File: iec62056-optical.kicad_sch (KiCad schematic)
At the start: 5 parts, among them J1 Conn_01x04_Male, Q1 Q_Photo_NPN

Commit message: version 1.0
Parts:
- D1: value LED -> IR42-21C; LCSC (none) -> C131198
- Q1: value Q_Photo_NPN -> PT42-21B; LCSC (none) -> C131199
- R1: value R -> 22R; LCSC (none) -> C23345
- R2: value R -> 1k8; LCSC (none) -> C4177
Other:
- moved on the sheet: D1, Q1, R1, R2

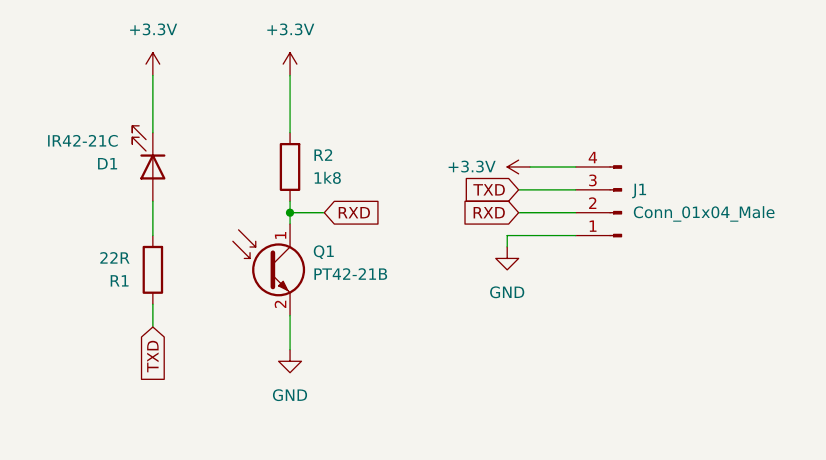
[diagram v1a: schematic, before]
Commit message: oprava orientace diody
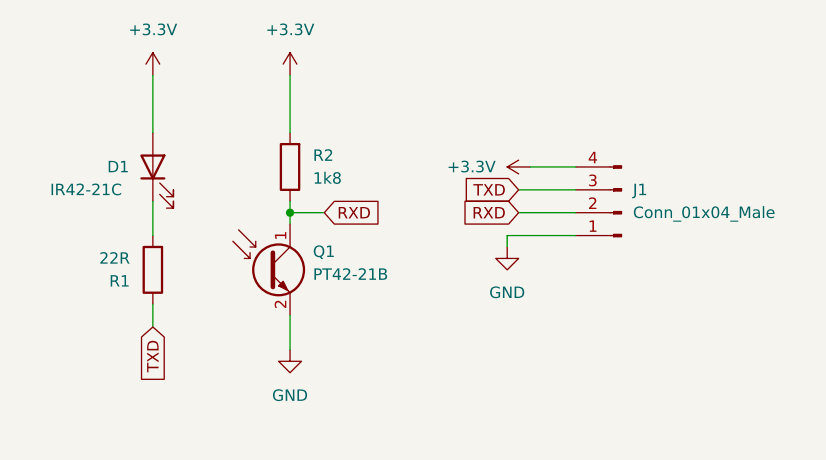
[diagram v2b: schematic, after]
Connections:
- net +3V3: now also D1.2 (A); no longer D1.1 (K)
- net at R1.2: now also D1.1 (K); no longer D1.2 (A)
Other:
- moved on the sheet: D1
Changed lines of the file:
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@@
     (pin "2")
   )
-  (symbol (lib_id "Device:LED") (at 107.95 81.28 270) (unit 1)
-    (in_bom yes) (on_board yes) (fields_autoplaced)
-    (property "Reference" "D1" (id 0) (at 104.14 80.9626 90)
+  (symbol (lib_id "Device:LED") (at 107.95 81.28 90) (unit 1)
+    (in_bom yes) (on_board yes)
+    (property "Reference" "D1" (id 0) (at 102.87 81.28 90)
       (effects (font (size 1.27 1.27)) (justify right))
     )
-    (property "Value" "IR42-21C" (id 1) (at 104.14 78.4226 90)
+    (property "Value" "IR42-21C" (id 1) (at 96.52 83.82 90)
       (effects (font (size 1.27 1.27)) (justify right))
     )
